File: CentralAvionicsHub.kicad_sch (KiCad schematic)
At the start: 18 parts, among them J1 GPS/ARINC, J2 MFD, J3 PFD, J4 NavCom, J5 Airframe, J6 GND1, J7 GND2, J8 Power_In, J9 Switches_Indicators

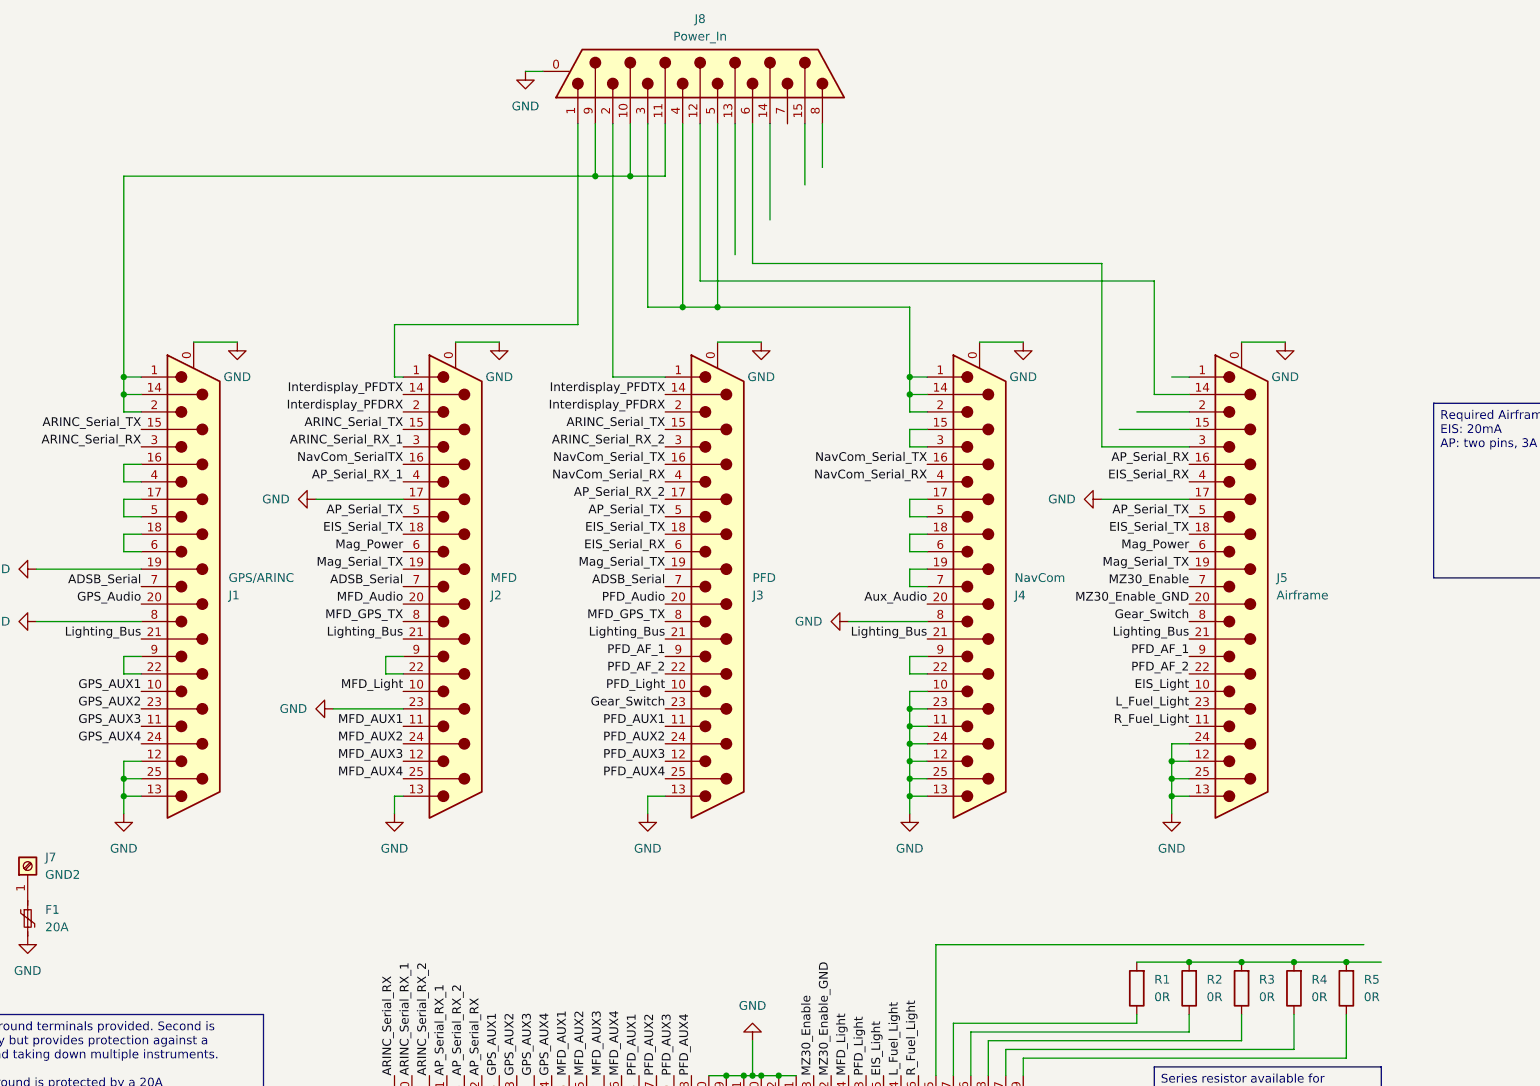
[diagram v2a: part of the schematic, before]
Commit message: Power routing mostly complete. Rearranged pinout on power_in connector to support better routing. Broke a number of other traces in the process, will correct later.
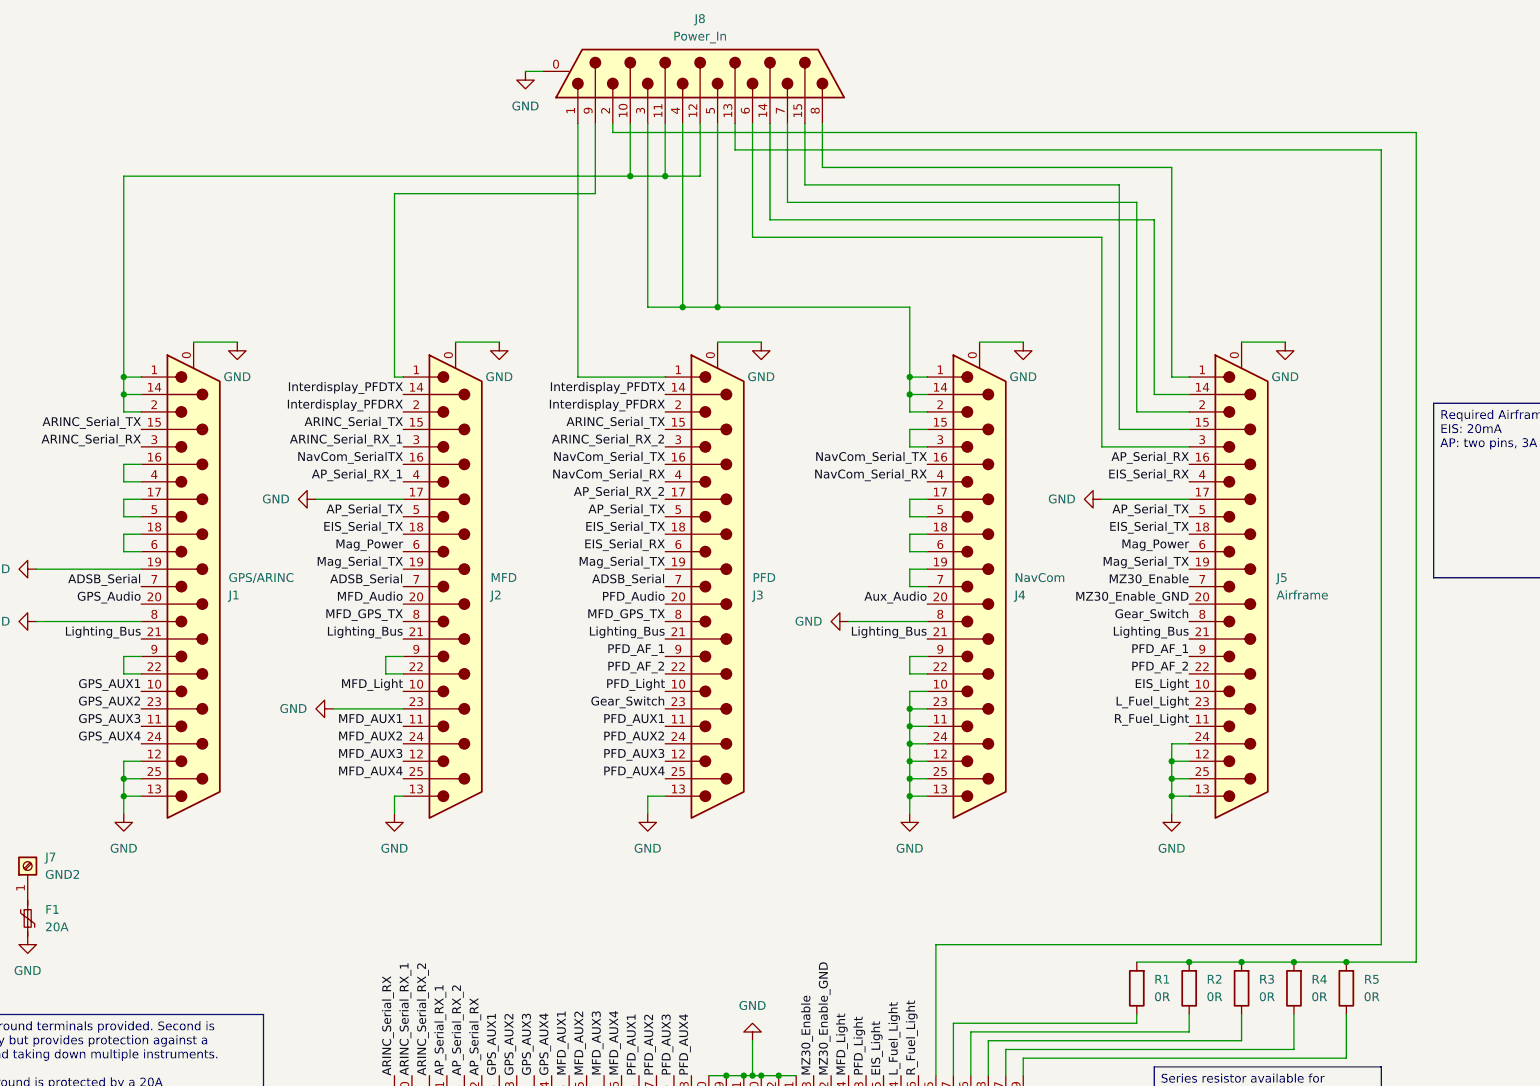
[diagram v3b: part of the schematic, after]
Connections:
- net at R1.2, R2.2, R3.2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: now also J8.2
- net at J8.1: now also J3.1; no longer J2.1
- net at J1.1, J1.14 (P14), J1.2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: now also J8.12 (P12); no longer J8.9 (P9)
- net at J5.14 (P14): now also J8.14 (P14); no longer J8.12 (P12)
- net at J8.13 (P13): now also J9.35
- net at J8.15 (P15): now also J5.15 (P15)
- net at J8.7: now also J5.2
- net at J8.8: now also J5.1
- new net: J2.1, J8.9 (P9)
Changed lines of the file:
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@@
-	)
-	(junction
-		(at 200.66 62.23)
-		(diameter 0)
-		(color 0 0 0 0)
 	)
 	(junction
@@
 	)
 	(junction
+		(at 210.82 62.23)
+		(diameter 0)
+		(color 0 0 0 0)
+	)
+	(junction
 		(at 302.26 176.53)
 		(diameter 0)
@@
 	(wire
 		(pts
-			(xy 200.66 62.23) (xy 132.08 62.23)
-		)
-		(stroke
-			(width 0)
-			(type default)
-		)
-	)
-	(wire
-		(pts
 			(xy 87.63 104.14) (xy 91.44 104.14)
 		)
@@
 	(wire
 		(pts
-			(xy 309.88 176.53) (xy 314.96 176.53)
+			(xy 309.88 176.53) (xy 320.04 176.53)
 		)
 		(stroke
@@
 	(wire
 		(pts
-			(xy 215.9 77.47) (xy 215.9 54.61)
-		)
-		(stroke
-			(width 0)
-			(type default)
-		)
-	)
-	(wire
-		(pts
 			(xy 142.24 86.36) (xy 148.59 86.36)
 		)
@@
 	(wire
 		(pts
-			(xy 203.2 91.44) (xy 203.2 54.61)
+			(xy 198.12 91.44) (xy 198.12 54.61)
 		)
 		(stroke
@@
 	(wire
 		(pts
-			(xy 281.94 77.47) (xy 215.9 77.47)
-		)
-		(stroke
-			(width 0)
-			(type default)
-		)
-	)
-	(wire
-		(pts
 			(xy 132.08 104.14) (xy 132.08 106.68)
 		)
@@
 	(wire
 		(pts
-			(xy 274.32 74.93) (xy 274.32 101.6)
+			(xy 274.32 71.12) (xy 274.32 101.6)
 		)
 		(stroke
@@
 	(wire
 		(pts
-			(xy 281.94 93.98) (xy 281.94 77.47)
+			(xy 281.94 93.98) (xy 281.94 68.58)
 		)
 		(stroke
@@
 	(wire
 		(pts
+			(xy 320.04 55.88) (xy 320.04 176.53)
+		)
+		(stroke
+			(width 0)
+			(type default)
+		)
+	)
+	(wire
+		(pts
 			(xy 246.38 116.84) (xy 248.92 116.84)
 		)
@@
 	(wire
 		(pts
+			(xy 284.48 60.96) (xy 284.48 91.44)
+		)
+		(stroke
+			(width 0)
+			(type default)
+		)
+	)
+	(wire
+		(pts
 			(xy 248.92 119.38) (xy 246.38 119.38)
 		)
@@
 	(wire
 		(pts
+			(xy 231.14 63.5) (xy 276.86 63.5)
+		)
+		(stroke
+			(width 0)
+			(type default)
+		)
+	)
+	(wire
+		(pts
 			(xy 302.26 176.53) (xy 309.88 176.53)
 		)
@@
 	(wire
 		(pts
+			(xy 228.6 66.04) (xy 279.4 66.04)
+		)
+		(stroke
+			(width 0)
+			(type default)
+		)
+	)
+	(wire
+		(pts
+			(xy 220.98 54.61) (xy 220.98 58.42)
+		)
+		(stroke
+			(width 0)
+			(type default)
+		)
+	)
+	(wire
+		(pts
 			(xy 246.38 152.4) (xy 246.38 154.94)
 		)
@@
 	(wire
 		(pts
+			(xy 203.2 54.61) (xy 203.2 55.88)
+		)
+		(stroke
+			(width 0)
+			(type default)
+		)
+	)
+	(wire
+		(pts
 			(xy 248.92 99.06) (xy 246.38 99.06)
 		)
@@
 	(wire
 		(pts
-			(xy 203.2 91.44) (xy 210.82 91.44)
-		)
-		(stroke
-			(width 0)
-			(type default)
-		)
-	)
-	(wire
-		(pts
 			(xy 279.4 185.42) (xy 279.4 184.15)
 		)
@@
 	(wire
 		(pts
-			(xy 200.66 54.61) (xy 200.66 62.23)
-		)
-		(stroke
-			(width 0)
-			(type default)
-		)
-	)
-	(wire
-		(pts
 			(xy 162.56 139.7) (xy 172.72 139.7)
 		)
@@
 	(wire
 		(pts
-			(xy 171.45 83.82) (xy 171.45 91.44)
+			(xy 171.45 64.77) (xy 171.45 91.44)
 		)
 		(stroke
@@
 	(wire
 		(pts
+			(xy 226.06 68.58) (xy 281.94 68.58)
+		)
+		(stroke
+			(width 0)
+			(type default)
+		)
+	)
+	(wire
+		(pts
 			(xy 287.02 149.86) (xy 284.48 149.86)
 		)
@@
 	(wire
 		(pts
+			(xy 233.68 60.96) (xy 284.48 60.96)
+		)
+		(stroke
+			(width 0)
+			(type default)
+		)
+	)
+	(wire
+		(pts
 			(xy 284.48 149.86) (xy 284.48 152.4)
 		)
@@
 	(wire
 		(pts
+			(xy 198.12 91.44) (xy 210.82 91.44)
+		)
+		(stroke
+			(width 0)
+			(type default)
+		)
+	)
+	(wire
+		(pts
 			(xy 302.26 189.23) (xy 302.26 184.15)
 		)
@@
 	(wire
 		(pts
-			(xy 312.42 173.99) (xy 250.19 173.99)
+			(xy 250.19 173.99) (xy 314.96 173.99)
 		)
 		(stroke
@@
 	(wire
 		(pts
+			(xy 279.4 66.04) (xy 279.4 96.52)
+		)
+		(stroke
+			(width 0)
+			(type default)
+		)
+	)
+	(wire
+		(pts
 			(xy 284.48 91.44) (xy 287.02 91.44)
 		)
@@
 	(wire
 		(pts
+			(xy 228.6 54.61) (xy 228.6 66.04)
+		)
+		(stroke
+			(width 0)
+			(type default)
+		)
+	)
+	(wire
+		(pts
 			(xy 210.82 62.23) (xy 205.74 62.23)
 		)
@@
 	(wire
 		(pts
-			(xy 205.74 62.23) (xy 200.66 62.23)
+			(xy 132.08 62.23) (xy 205.74 62.23)
 		)
 		(stroke
@@
 	(wire
 		(pts
-			(xy 171.45 83.82) (xy 198.12 83.82)
+			(xy 215.9 54.61) (xy 215.9 62.23)
+		)
+		(stroke
+			(width 0)
+			(type default)
+		)
+	)
+	(wire
+		(pts
+			(xy 171.45 64.77) (xy 200.66 64.77)
+		)
+		(stroke
+			(width 0)
+			(type default)
+		)
+	)
+	(wire
+		(pts
+			(xy 203.2 55.88) (xy 320.04 55.88)
 		)
 		(stroke
@@
 	(wire
 		(pts
+			(xy 314.96 58.42) (xy 314.96 173.99)
+		)
+		(stroke
+			(width 0)
+			(type default)
+		)
+	)
+	(wire
+		(pts
 			(xy 219.71 193.04) (xy 222.25 193.04)
 		)
@@
 	(wire
 		(pts
-			(xy 223.52 74.93) (xy 274.32 74.93)
+			(xy 223.52 71.12) (xy 274.32 71.12)
 		)
 		(stroke
@@
 	(wire
 		(pts
+			(xy 276.86 63.5) (xy 276.86 99.06)
+		)
+		(stroke
+			(width 0)
+			(type default)
+		)
+	)
+	(wire
+		(pts
 			(xy 287.02 101.6) (xy 274.32 101.6)
 		)
@@
 	(wire
 		(pts
-			(xy 198.12 83.82) (xy 198.12 54.61)
+			(xy 200.66 64.77) (xy 200.66 54.61)
 		)
 		(stroke
@@
 	(wire
 		(pts
+			(xy 220.98 58.42) (xy 314.96 58.42)
+		)
+		(stroke
+			(width 0)
+			(type default)
+		)
+	)
+	(wire
+		(pts
 			(xy 224.79 193.04) (xy 227.33 193.04)
 		)
@@
 	(wire
 		(pts
-			(xy 220.98 73.66) (xy 220.98 54.61)
-		)
-		(stroke
-			(width 0)
-			(type default)
-		)
-	)
-	(wire
-		(pts
 			(xy 246.38 137.16) (xy 246.38 139.7)
 		)
@@
 	(wire
 		(pts
+			(xy 215.9 62.23) (xy 210.82 62.23)
+		)
+		(stroke
+			(width 0)
+			(type default)
+		)
+	)
+	(wire
+		(pts
 			(xy 132.08 93.98) (xy 134.62 93.98)
 		)
@@
 	(wire
 		(pts
-			(xy 223.52 54.61) (xy 223.52 74.93)
-		)
-		(stroke
+			(xy 223.52 54.61) (xy 223.52 71.12)
+		)
+		(stroke

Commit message: Minor Fixes, silkscreen updates.
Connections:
- net NavCom_SerialTX is gone; now on net NavCom_Serial_TX: J2.16 (P16)
- net Annunciator_V+: now reaches J8.2, R1.2, R2.2, R3.2, R4.2, R5.2
- net PFD_V+: now reaches J3.1, J8.1
- net GPS_V+: now reaches J1.1, J1.14 (P14), J1.2, J8.10 (P10), J8.11 (P111), J8.12 (P12)
- net Spare_Switchpanel_V+: now reaches J8.13 (P13), J9.35
- net Pitch_Servo_V+: now reaches J5.14 (P14), J8.14 (P14)
- net AF_Spare_V+_2: now reaches J5.15 (P15), J8.15 (P15)
- net NavCom_V+: now reaches J4.1, J4.14 (P14), J4.2, J8.3, J8.4, J8.5
- net AF_Spare_V+_3: now reaches J5.3, J8.6
- net AF_Spare_V+_1: now reaches J5.2, J8.7
- net Roll_Servo_V+: now reaches J5.1, J8.8
- net MFD_V+: now reaches J2.1, J8.9 (P9)
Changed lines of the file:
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@@
+		)
+	)
+	(label "PFD_V+"
+		(at 200.66 91.44 0)
+		(effects
+			(font
+				(size 1.27 1.27)
+			)
+			(justify left bottom)
 		)
 	)
@@
 		)
 	)
+	(label "AF_Spare_V+_3"
+		(at 251.3928 71.12 0)
+		(effects
+			(font
+				(size 1.27 1.27)
+			)
+			(justify left bottom)
+		)
+	)
 	(label "AP_Serial_RX_1"
 		(at 179.07 193.04 90)
@@
 		)
 	)
+	(label "MFD_V+"
+		(at 177.8 64.77 0)
+		(effects
+			(font
+				(size 1.27 1.27)
+			)
+			(justify left bottom)
+		)
+	)
 	(label "ARINC_Serial_RX_1"
 		(at 172.72 101.6 180)
@@
 		)
 	)
+	(label "AF_Spare_V+_2"
+		(at 251.46 63.5 0)
+		(effects
+			(font
+				(size 1.27 1.27)
+			)
+			(justify left bottom)
+		)
+	)
+	(label "Pitch_Servo_V+"
+		(at 251.46 68.58 0)
+		(effects
+			(font
+				(size 1.27 1.27)
+			)
+			(justify left bottom)
+		)
+	)
 	(label "AP_Serial_RX"
 		(at 287.02 104.14 180)
@@
 		)
 	)
+	(label "Spare_Switchpanel_V+"
+		(at 251.46 58.42 0)
+		(effects
+			(font
+				(size 1.27 1.27)
+			)
+			(justify left bottom)
+		)
+	)
+	(label "NavCom_V+"
+		(at 227.33 81.28 0)
+		(effects
+			(font
+				(size 1.27 1.27)
+			)
+			(justify left bottom)
+		)
+	)
 	(label "EIS_Light"
 		(at 287.02 137.16 180)
@@
 		)
 	)
-	(label "NavCom_SerialTX"
+	(label "NavCom_Serial_TX"
 		(at 172.72 104.14 180)
 		(effects
@@
 		)
 	)
+	(label "Annunciator_V+"
+		(at 251.46 55.88 0)
+		(effects
+			(font
+				(size 1.27 1.27)
+			)
+			(justify left bottom)
+		)
+	)
 	(label "L_Fuel_Light"
 		(at 245.11 193.04 90)
@@
 		(effects
 			(font
+				(size 1.27 1.27)
+			)
+			(justify left bottom)
+		)
+	)
+	(label "AF_Spare_V+_1"
+		(at 251.46 66.04 0)
+		(effects
+			(font
+				(size 1.27 1.27)
+			)
+			(justify left bottom)
+		)
+	)
+	(label "GPS_V+"
+		(at 146.05 62.23 0)
+		(effects
+			(font
+				(size 1.27 1.27)
+			)
+			(justify left bottom)
+		)
+	)
+	(label "Roll_Servo_V+"
+		(at 251.46 60.96 0)
+		(effects
+			(font

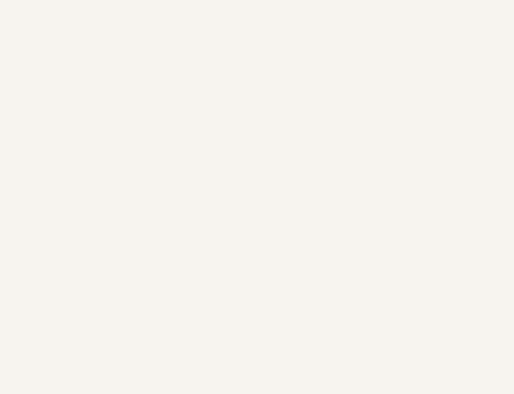
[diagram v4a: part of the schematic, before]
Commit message: Changed Ground connections to 250 FASTON tabs. Updated silkscreen. Corrected minor DRC errors.
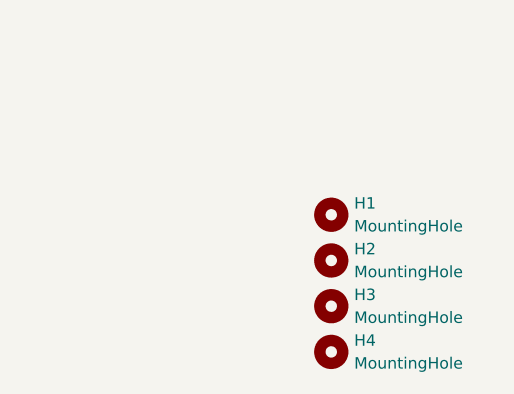
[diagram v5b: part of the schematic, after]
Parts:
- added H1, H2, H3, H4: MountingHole, MountingHole:MountingHole_4.3mm_M4_ISO7380, symbol Mechanical:MountingHole
- J6, J7: footprint MountingHole:MountingHole_4mm_Pad_TopBottom -> FASTON_TAB:63824
